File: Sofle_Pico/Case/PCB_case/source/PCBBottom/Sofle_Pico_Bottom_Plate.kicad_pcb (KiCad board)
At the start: 2 copper layers, 145.4 x 116.3 mm, 41 parts, among them SW1 SW_PUSH_LED, SW10 SW_PUSH_LED, SW11 SW_PUSH_LED, SW12 SW_PUSH_LED, SW13 SW_PUSH_LED, SW14 SW_PUSH_LED, SW15 SW_PUSH_LED, SW16 SW_PUSH_LED, SW17 SW_PUSH_LED, SW18 SW_PUSH_LED, SW19 SW_PUSH_LED, SW2 SW_PUSH_LED, SW20 SW_PUSH_LED, SW21 SW_PUSH_LED, SW22 SW_PUSH_LED, SW23 SW_PUSH_LED, SW24 SW_PUSH_LED, SW25 Rotary_Encoder_Switch-Device, SW26 SW_PUSH_LED, SW27 SW_PUSH_LED, SW28 SW_PUSH_LED, SW29 SW_PUSH_LED, SW3 SW_PUSH_LED, SW30 SW_PUSH_LED, SW4 SW_PUSH_LED, SW5 SW_PUSH_LED, SW6 SW_PUSH_LED, SW7 SW_PUSH_LED, SW8 SW_PUSH_LED, SW9 SW_PUSH_LED

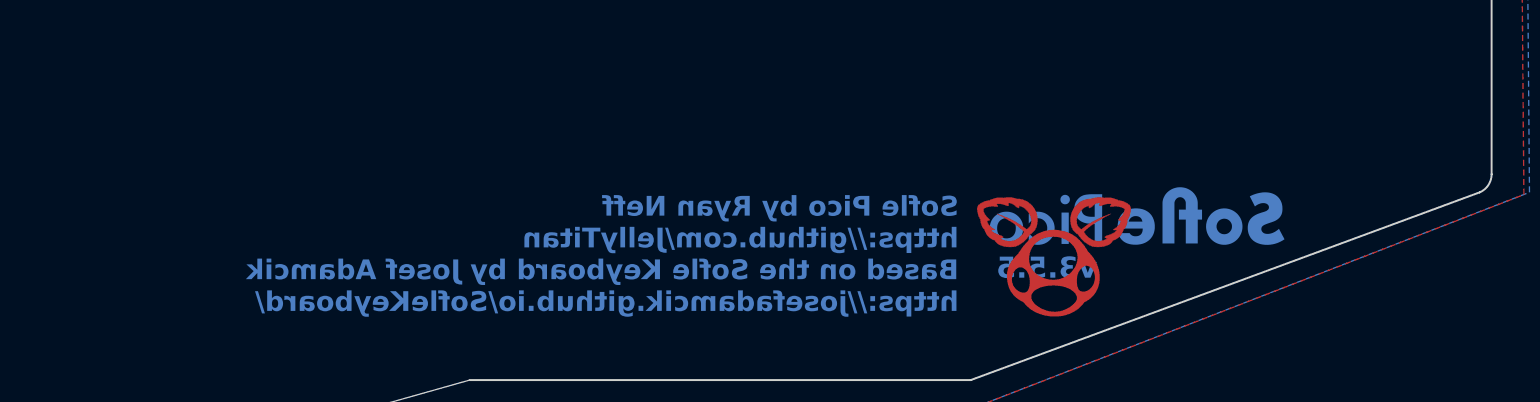
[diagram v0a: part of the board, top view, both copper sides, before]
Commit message: Finished pcb case - ready for testing generated gerbers created backplate variant without tenting puck hole dialed in back plate branding
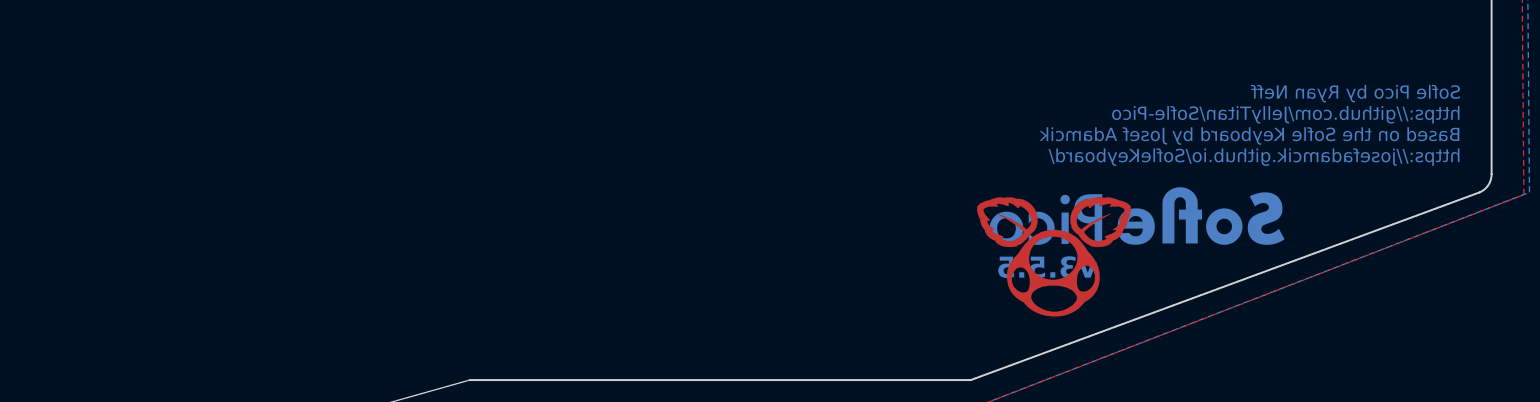
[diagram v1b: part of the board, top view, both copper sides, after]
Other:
- board text added: "Sofle Pico by Ryan Neff https://github.com/JellyTitan/Sofle-Pico Based on the Sofle Keyboard by Josef Adamcik https://josefadamcik.github.io/SofleKeyboard/"
- board text removed: "Sofle Pico by Ryan Neff https://github.com/JellyTitan Based on the Sofle Keyboard by Josef Adamcik https://josefadamcik.github.io/SofleKeyboard/"
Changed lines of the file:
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@@
       (outputformat 1)
       (mirror false)
-      (drillshape 1)
+      (drillshape 0)
       (scaleselection 1)
-      (outputdirectory "")
+      (outputdirectory "Gerbers_puckhole/")
     )
   )
@@
   (gr_arc (start 108.805 99.895001) (mid 108.512106 100.602107) (end 107.805 100.895001)
     (stroke (width 0.1) (type default)) (layer "User.8"))
-  (gr_text "Sofle Pico by Ryan Neff\nhttps://github.com/JellyTitan\nBased on the Sofle Keyboard by Josef Adamcik\nhttps://josefadamcik.github.io/SofleKeyboard/" (at 184.3 136.175) (layer "B.Cu" knockout)
-    (effects (font (size 1.5 1.5) (thickness 0.375) bold) (justify left bottom mirror))
+  (gr_text "Sofle Pico by Ryan Neff\nhttps://github.com/JellyTitan/Sofle-Pico\nBased on the Sofle Keyboard by Josef Adamcik\nhttps://josefadamcik.github.io/SofleKeyboard/" (at 222.5 124.8) (layer "B.Cu")
+    (effects (font (size 1 1) (thickness 0.125)) (justify left bottom mirror))
   )
   (gr_text "v${REVISION}" (at 187.15 132.725) (layer "B.Cu")
